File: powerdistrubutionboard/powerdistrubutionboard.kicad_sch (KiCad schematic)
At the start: 16 parts

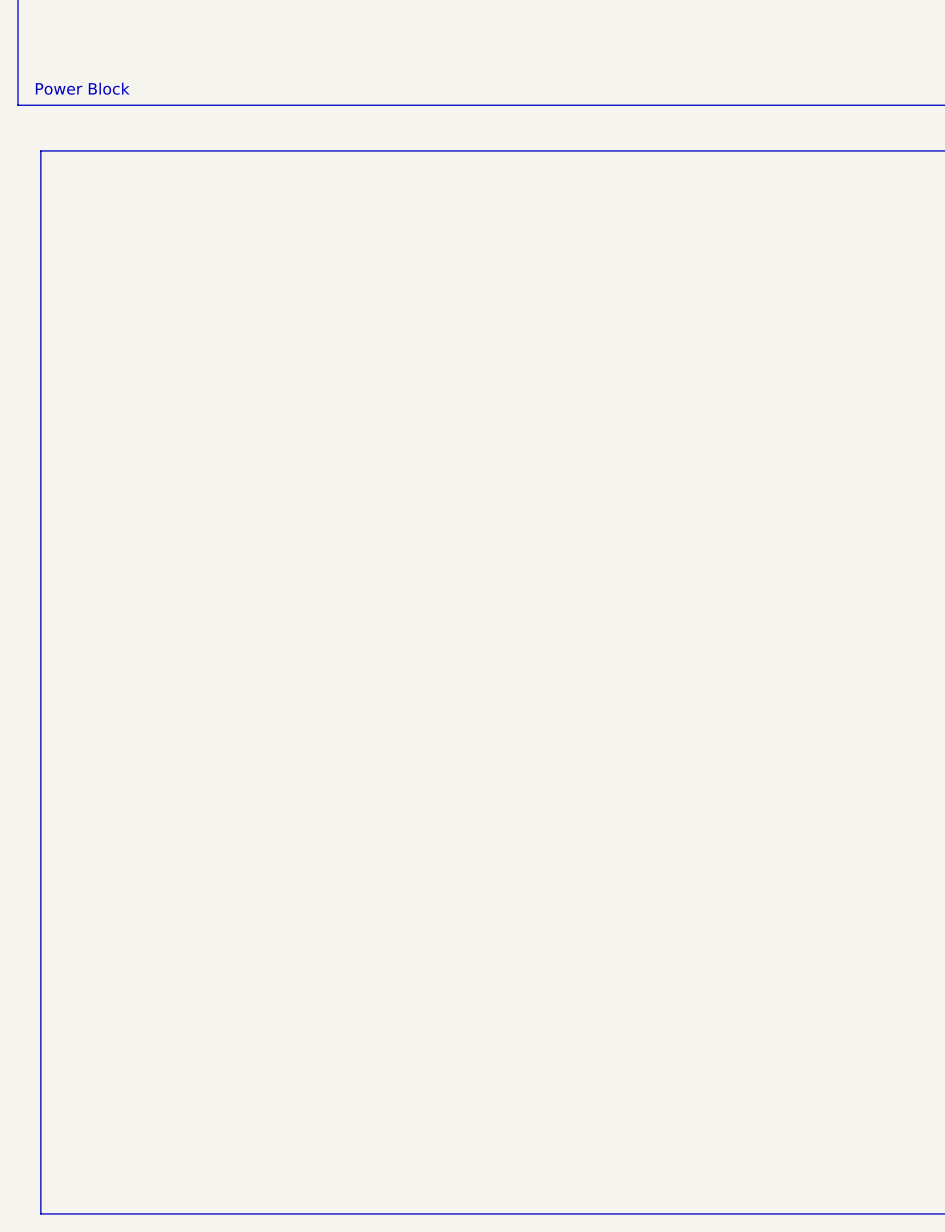
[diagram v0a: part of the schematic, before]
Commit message: update the 3 phase bridge for ESC
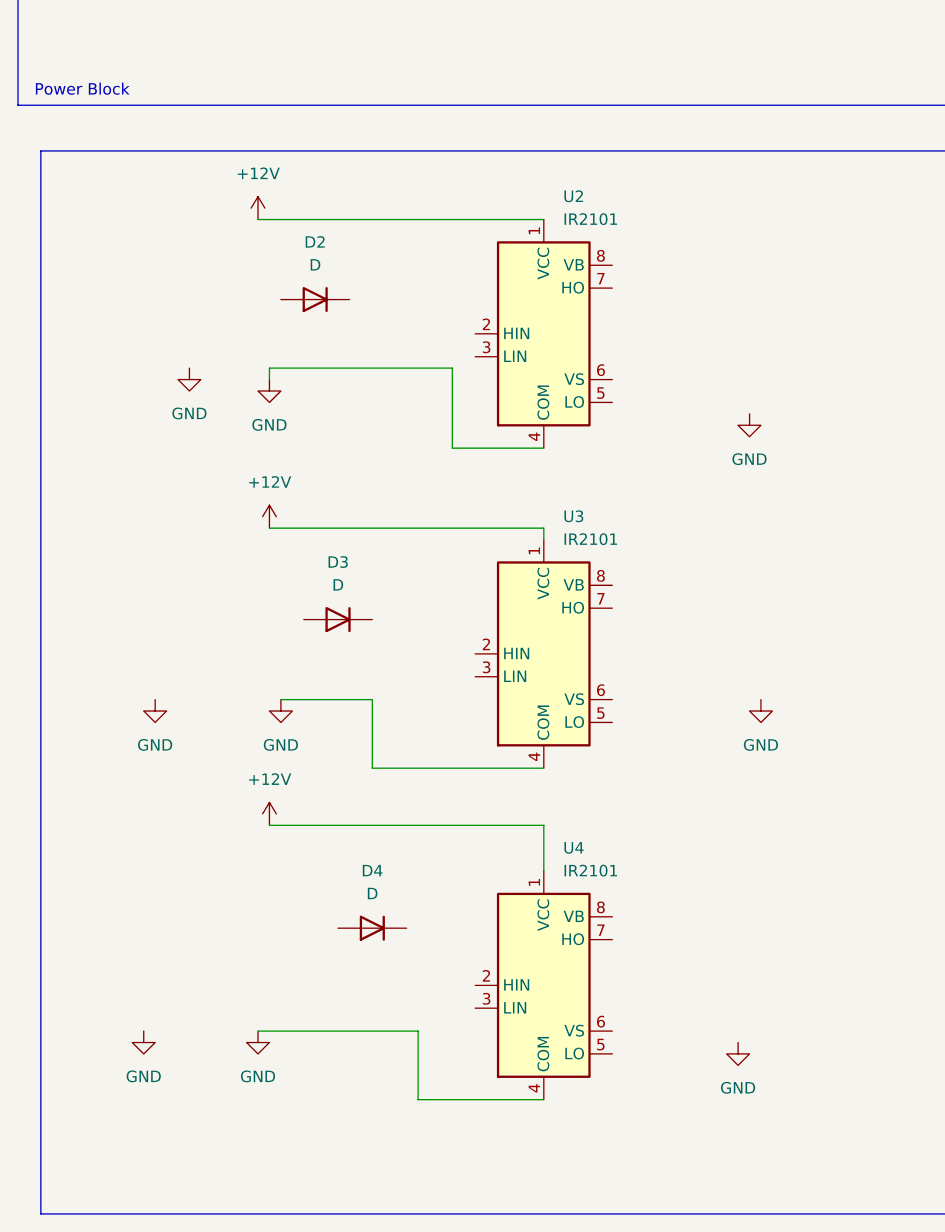
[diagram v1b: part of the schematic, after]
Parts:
- added D2, D3, D4: D, symbol Device:D
- added U2, U3, U4: IR2101, symbol Driver_FET:IR2101
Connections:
- net +12V: now also U2.1 (VCC), U3.1 (VCC), U4.1 (VCC)
- net GND: now also U2.4 (COM), U3.4 (COM), U4.4 (COM)
